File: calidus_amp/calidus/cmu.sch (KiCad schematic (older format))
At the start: 21 parts, among them Q1 Q_NPN_CBE, Q2 Q_NPN_CBE, Q3 Q_NPN_CBE, U6 PIC18F26K40_ISP

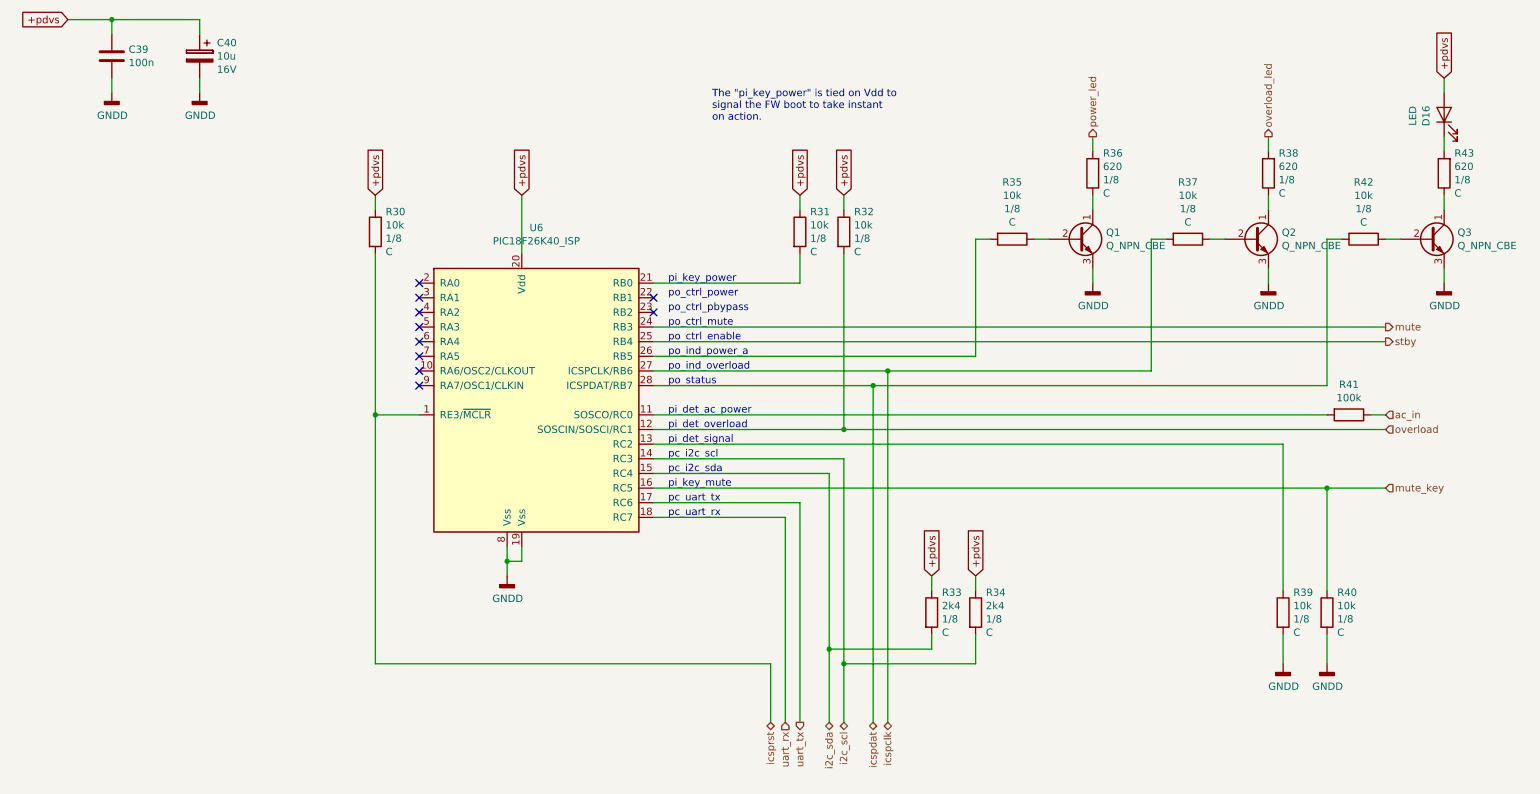
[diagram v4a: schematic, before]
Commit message: WIP: Component placement on PCB
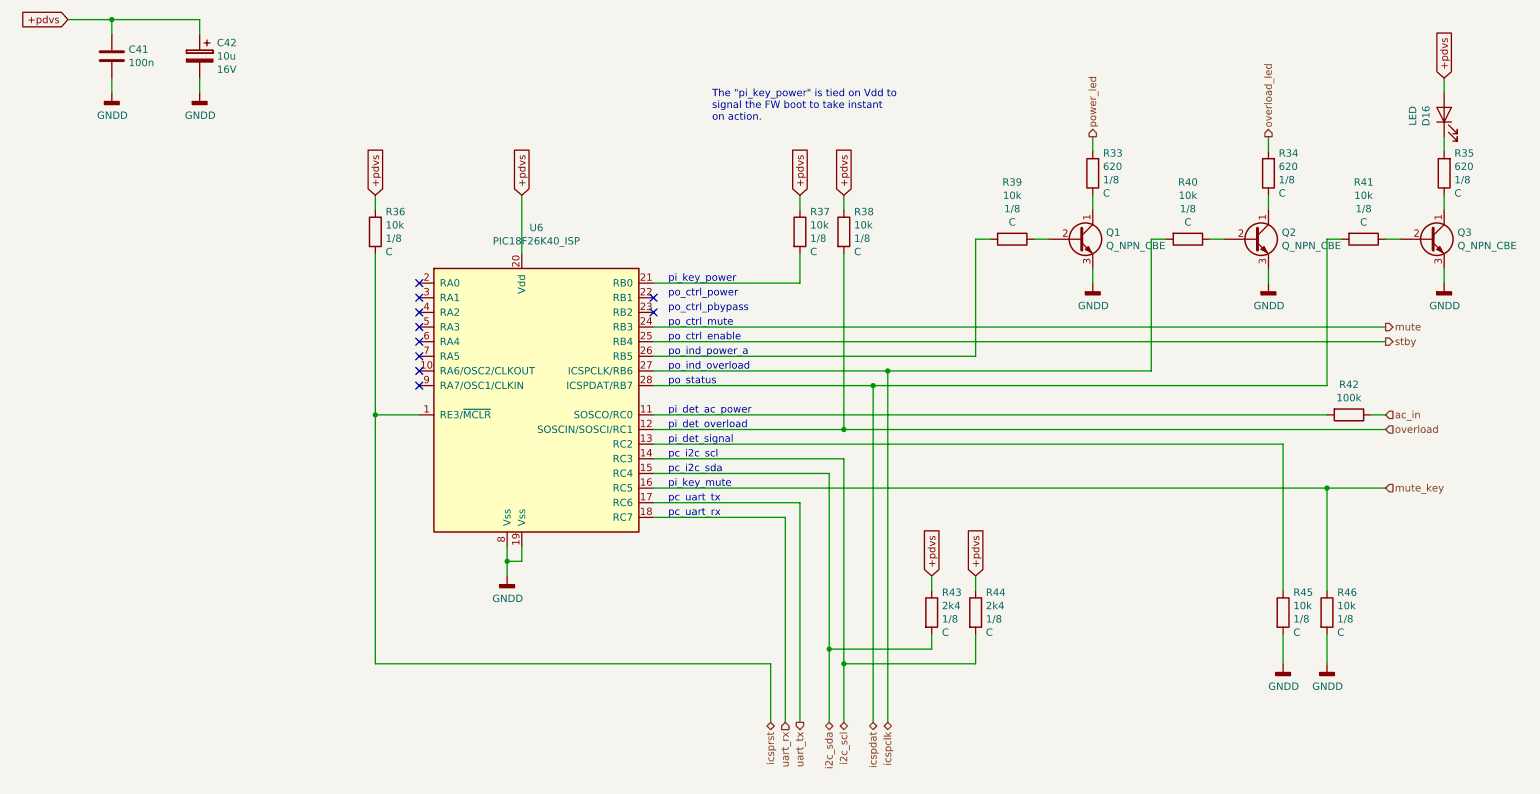
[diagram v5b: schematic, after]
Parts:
- renumbered C39 to C41, C40 to C42, R36 to R33, R38 to R34, R43 to R35, R30 to R36, R31 to R37, R32 to R38, R35 to R39, R37 to R40, R42 to R41, R41 to R42, R33 to R43, R34 to R44, R39 to R45, R40 to R46
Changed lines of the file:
@@
 $Descr A4 11693 8268
 encoding utf-8
-Sheet 5 4
+Sheet 4 4
 Title ""
 Date ""
@@
 $EndDescr
 $Comp
-L power:GNDD #PWR031
+L power:GNDD #PWR028
 U 1 1 5C444574
 P 4200 5200
-F 0 "#PWR031" H 4200 4950 50  0001 C CNN
+F 0 "#PWR028" H 4200 4950 50  0001 C CNN
 F 1 "GNDD" H 4204 5045 50  0000 C CNN
 F 2 "" H 4200 5200 50  0001 C CNN
@@
 	1500 1400 1500 1500
 $Comp
-L power:GNDD #PWR029
+L power:GNDD #PWR023
 U 1 1 5C444792
 P 1500 1900
-F 0 "#PWR029" H 1500 1650 50  0001 C CNN
+F 0 "#PWR023" H 1500 1650 50  0001 C CNN
 F 1 "GNDD" H 1504 1745 50  0000 C CNN
 F 2 "" H 1500 1900 50  0001 C CNN
@@
 $EndComp
 $Comp
-L Device:C C39
+L Device:C C41
 U 1 1 5C46D3BF
 P 1500 1650
-F 0 "C39" H 1615 1696 50  0000 L CNN
+F 0 "C41" H 1615 1696 50  0000 L CNN
 F 1 "100n" H 1615 1605 50  0000 L CNN
 F 2 "Capacitor_THT:C_Rect_L7.0mm_W2.5mm_P5.00mm" H 1538 1500 50  0001 C CNN
@@
 NoConn ~ 5200 3300
 $Comp
-L Device:R R36
+L Device:R R33
 U 1 1 5C48301D
 P 8200 2450
-F 0 "R36" H 8130 2313 50  0000 R CNN
+F 0 "R33" H 8130 2313 50  0000 R CNN
 F 1 "620" H 8130 2404 50  0000 R CNN
 F 2 "Resistor_THT:R_Axial_DIN0204_L3.6mm_D1.6mm_P5.08mm_Horizontal" V 8130 2450 50  0001 C CNN
@@
 $EndComp
 $Comp
-L power:GNDD #PWR032
+L power:GNDD #PWR025
 U 1 1 5C4835A2
 P 8200 3200
-F 0 "#PWR032" H 8200 2950 50  0001 C CNN
+F 0 "#PWR025" H 8200 2950 50  0001 C CNN
 F 1 "GNDD" H 8204 3045 50  0000 C CNN
 F 2 "" H 8200 3200 50  0001 C CNN
@@
 	8200 3200 8200 3100
 $Comp
-L power:GNDD #PWR033
+L power:GNDD #PWR026
 U 1 1 5C46343D
 P 9400 3200
-F 0 "#PWR033" H 9400 2950 50  0001 C CNN
+F 0 "#PWR026" H 9400 2950 50  0001 C CNN
 F 1 "GNDD" H 9404 3045 50  0000 C CNN
 F 2 "" H 9400 3200 50  0001 C CNN
@@
 $EndComp
 $Comp
-L power:GNDD #PWR036
+L power:GNDD #PWR027
 U 1 1 5C463464
 P 10600 3200
-F 0 "#PWR036" H 10600 2950 50  0001 C CNN
+F 0 "#PWR027" H 10600 2950 50  0001 C CNN
 F 1 "GNDD" H 10604 3045 50  0000 C CNN
 F 2 "" H 10600 3200 50  0001 C CNN
@@
 	9800 2900 9900 2900
 $Comp
-L Device:R R30
+L Device:R R36
 U 1 1 5C4640C2
 P 3300 2850
-F 0 "R30" H 3370 2987 50  0000 L CNN
+F 0 "R36" H 3370 2987 50  0000 L CNN
 F 1 "10k" H 3370 2896 50  0000 L CNN
 F 2 "Resistor_THT:R_Axial_DIN0204_L3.6mm_D1.6mm_P5.08mm_Horizontal" V 3230 2850 50  0001 C CNN
@@
 	10200 4200 6500 4200
 $Comp
-L Device:R R41
+L Device:R R42
 U 1 1 5C466052
 P 9950 4100
-F 0 "R41" V 9743 4100 50  0000 C CNN
+F 0 "R42" V 9743 4100 50  0000 C CNN
 F 1 "100k" V 9834 4100 50  0000 C CNN
 F 2 "Resistor_THT:R_Axial_DIN0207_L6.3mm_D2.5mm_P7.62mm_Horizontal" V 9880 4100 50  0001 C CNN
@@
 	6500 4400 5200 4400
 $Comp
-L power:GNDD #PWR034
+L power:GNDD #PWR029
 U 1 1 5C475E16
 P 9500 5800
-F 0 "#PWR034" H 9500 5550 50  0001 C CNN
+F 0 "#PWR029" H 9500 5550 50  0001 C CNN
 F 1 "GNDD" H 9504 5645 50  0000 C CNN
 F 2 "" H 9500 5800 50  0001 C CNN
@@
 $EndComp
 $Comp
-L power:GNDD #PWR035
+L power:GNDD #PWR030
 U 1 1 5C476CD2
 P 9800 5800
-F 0 "#PWR035" H 9800 5550 50  0001 C CNN
+F 0 "#PWR030" H 9800 5550 50  0001 C CNN
 F 1 "GNDD" H 9804 5645 50  0000 C CNN
 F 2 "" H 9800 5800 50  0001 C CNN
@@
 $EndComp
 $Comp
-L Device:R R33
+L Device:R R43
 U 1 1 5C477BD2
 P 7100 5450
-F 0 "R33" H 7170 5587 50  0000 L CNN
+F 0 "R43" H 7170 5587 50  0000 L CNN
 F 1 "2k4" H 7170 5496 50  0000 L CNN
 F 2 "Resistor_THT:R_Axial_DIN0204_L3.6mm_D1.6mm_P5.08mm_Horizontal" V 7030 5450 50  0001 C CNN
@@
 	6500 4200 5200 4200
 $Comp
-L Device:R R31
+L Device:R R37
 U 1 1 5C4C2301
 P 6200 2850
-F 0 "R31" H 6270 2987 50  0000 L CNN
+F 0 "R37" H 6270 2987 50  0000 L CNN
 F 1 "10k" H 6270 2896 50  0000 L CNN
 F 2 "Resistor_THT:R_Axial_DIN0204_L3.6mm_D1.6mm_P5.08mm_Horizontal" V 6130 2850 50  0001 C CNN
@@
 $EndComp
 $Comp
-L Device:R R32
+L Device:R R38
 U 1 1 5C4C234B
 P 6500 2850
-F 0 "R32" H 6570 2987 50  0000 L CNN
+F 0 "R38" H 6570 2987 50  0000 L CNN
 F 1 "10k" H 6570 2896 50  0000 L CNN
 F 2 "Resistor_THT:R_Axial_DIN0204_L3.6mm_D1.6mm_P5.08mm_Horizontal" V 6430 2850 50  0001 C CNN
@@
 $EndComp
 $Comp
-L Device:R R39
+L Device:R R45
 U 1 1 5C4C2657
 P 9500 5450
-F 0 "R39" H 9570 5587 50  0000 L CNN
+F 0 "R45" H 9570 5587 50  0000 L CNN
 F 1 "10k" H 9570 5496 50  0000 L CNN
 F 2 "Resistor_THT:R_Axial_DIN0204_L3.6mm_D1.6mm_P5.08mm_Horizontal" V 9430 5450 50  0001 C CNN
@@
 $EndComp
 $Comp
-L Device:R R40
+L Device:R R46
 U 1 1 5C4C26B7
 P 9800 5450
-F 0 "R40" H 9870 5587 50  0000 L CNN
+F 0 "R46" H 9870 5587 50  0000 L CNN
 F 1 "10k" H 9870 5496 50  0000 L CNN
 F 2 "Resistor_THT:R_Axial_DIN0204_L3.6mm_D1.6mm_P5.08mm_Horizontal" V 9730 5450 50  0001 C CNN
@@
 $EndComp
 $Comp
-L Device:R R35
+L Device:R R39
 U 1 1 5C4C2732
 P 7650 2900
-F 0 "R35" V 7261 2900 50  0000 C CNN
+F 0 "R39" V 7261 2900 50  0000 C CNN
 F 1 "10k" V 7352 2900 50  0000 C CNN
 F 2 "Resistor_THT:R_Axial_DIN0204_L3.6mm_D1.6mm_P5.08mm_Horizontal" V 7580 2900 50  0001 C CNN
@@
 $EndComp
 $Comp
-L Device:R R37
+L Device:R R40
 U 1 1 5C4C2878
 P 8850 2900
-F 0 "R37" V 8461 2900 50  0000 C CNN
+F 0 "R40" V 8461 2900 50  0000 C CNN
 F 1 "10k" V 8552 2900 50  0000 C CNN
 F 2 "Resistor_THT:R_Axial_DIN0204_L3.6mm_D1.6mm_P5.08mm_Horizontal" V 8780 2900 50  0001 C CNN
@@
 $EndComp
 $Comp
-L Device:R R42
+L Device:R R41
 U 1 1 5C4C28CE
 P 10050 2900
-F 0 "R42" V 9661 2900 50  0000 C CNN
+F 0 "R41" V 9661 2900 50  0000 C CNN
 F 1 "10k" V 9752 2900 50  0000 C CNN
 F 2 "Resistor_THT:R_Axial_DIN0204_L3.6mm_D1.6mm_P5.08mm_Horizontal" V 9980 2900 50  0001 C CNN
@@
 P 2100 1650
 AR Path="/5C37BC7C/5C4C9FCF" Ref="C?"  Part="1"
-AR Path="/5C43C4AB/5C4C9FCF" Ref="C40"  Part="1"
-F 0 "C40" H 1982 1741 50  0000 R CNN
+AR Path="/5C43C4AB/5C4C9FCF" Ref="C42"  Part="1"
+F 0 "C42" H 1982 1741 50  0000 R CNN
 F 1 "10u" H 1982 1650 50  0000 R CNN
 F 2 "Capacitor_THT:CP_Radial_D5.0mm_P2.00mm" H 2138 1500 50  0001 C CNN
@@
 $EndComp
 $Comp
-L power:GNDD #PWR030
+L power:GNDD #PWR024
 U 1 1 5C4CB7C3
 P 2100 1900
-F 0 "#PWR030" H 2100 1650 50  0001 C CNN
+F 0 "#PWR024" H 2100 1650 50  0001 C CNN
 F 1 "GNDD" H 2104 1745 50  0000 C CNN
 F 2 "" H 2100 1900 50  0001 C CNN
@@
 Connection ~ 1500 1400
 $Comp
-L Device:R R34
+L Device:R R44
 U 1 1 5C4F79CD
 P 7400 5450
-F 0 "R34" H 7470 5587 50  0000 L CNN
+F 0 "R44" H 7470 5587 50  0000 L CNN
 F 1 "2k4" H 7470 5496 50  0000 L CNN
 F 2 "Resistor_THT:R_Axial_DIN0204_L3.6mm_D1.6mm_P5.08mm_Horizontal" V 7330 5450 50  0001 C CNN
@@
 $EndComp
 $Comp
-L Device:R R38
+L Device:R R34
 U 1 1 5C4F9272
 P 9400 2450
-F 0 "R38" H 9330 2313 50  0000 R CNN
+F 0 "R34" H 9330 2313 50  0000 R CNN
 F 1 "620" H 9330 2404 50  0000 R CNN
 F 2 "Resistor_THT:R_Axial_DIN0204_L3.6mm_D1.6mm_P5.08mm_Horizontal" V 9330 2450 50  0001 C CNN
@@
 $EndComp
 $Comp
-L Device:R R43
+L Device:R R35
 U 1 1 5C4F92B8
 P 10600 2450
-F 0 "R43" H 10530 2313 50  0000 R CNN
+F 0 "R35" H 10530 2313 50  0000 R CNN
 F 1 "620" H 10530 2404 50  0000 R CNN
 F 2 "Resistor_THT:R_Axial_DIN0204_L3.6mm_D1.6mm_P5.08mm_Horizontal" V 10530 2450 50  0001 C CNN

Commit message: WIP: Component placement
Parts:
- renumbered C41 to C45, C42 to C46
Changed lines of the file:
@@
 $EndComp
 $Comp
-L Device:C C41
+L Device:C C45
 U 1 1 5C46D3BF
 P 1500 1650
-F 0 "C41" H 1615 1696 50  0000 L CNN
+F 0 "C45" H 1615 1696 50  0000 L CNN
 F 1 "100n" H 1615 1605 50  0000 L CNN
 F 2 "Capacitor_THT:C_Rect_L7.0mm_W2.5mm_P5.00mm" H 1538 1500 50  0001 C CNN
@@
 P 2100 1650
 AR Path="/5C37BC7C/5C4C9FCF" Ref="C?"  Part="1"
-AR Path="/5C43C4AB/5C4C9FCF" Ref="C42"  Part="1"
-F 0 "C42" H 1982 1741 50  0000 R CNN
+AR Path="/5C43C4AB/5C4C9FCF" Ref="C46"  Part="1"
+F 0 "C46" H 1982 1741 50  0000 R CNN
 F 1 "10u" H 1982 1650 50  0000 R CNN
 F 2 "Capacitor_THT:CP_Radial_D5.0mm_P2.00mm" H 2138 1500 50  0001 C CNN

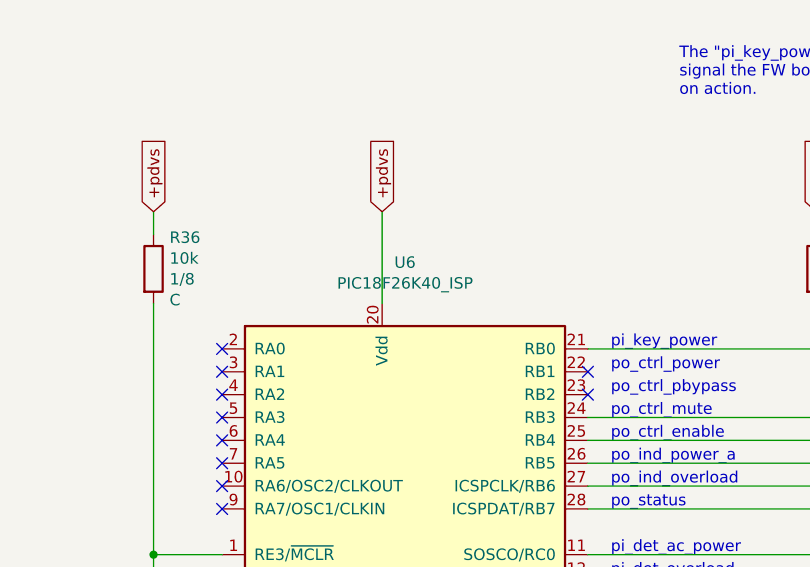
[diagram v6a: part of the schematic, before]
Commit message: WIP: Component placement and footprint assignement
- Finished all capacitors
- Finished all ICs
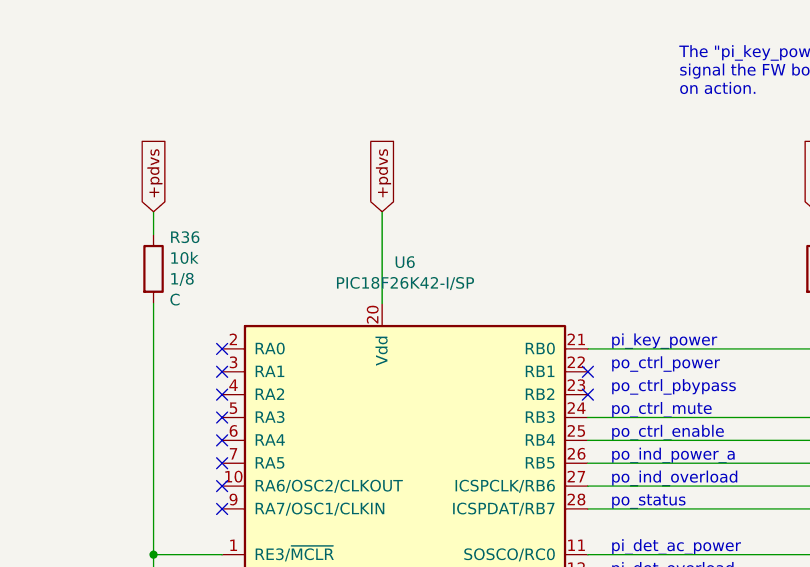
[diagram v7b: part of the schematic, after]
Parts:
- C45: footprint Capacitor_THT:C_Rect_L7.0mm_W2.5mm_P5.00mm -> Capacitor_THT:C_Rect_L4.6mm_W3.0mm_P2.50mm_MKS02_FKP02; Manufacturer (none) -> WIMA:MKS0C031000C00KSSD; Supplier1 (none) -> Farnell:1006004; Type (none) -> PET; Voltage (none) -> 63V
- R42: footprint Resistor_THT:R_Axial_DIN0207_L6.3mm_D2.5mm_P7.62mm_Horizontal -> Resistor_THT:R_Axial_DIN0204_L3.6mm_D1.6mm_P5.08mm_Horizontal; Manufacturer (none) -> Multicomp:MF12 10K; Power (none) -> 1/8; Supplier1 (none) -> Farnell:9342427; Type (none) -> C
- U6: value PIC18F26K40_ISP -> PIC18F26K42-I/SP; Manufacturer (none) -> Microchip:PIC18F26K42-I/SP; Supplier1 (none) -> Farnell:2835929
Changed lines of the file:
@@
 F 0 "C45" H 1615 1696 50  0000 L CNN
 F 1 "100n" H 1615 1605 50  0000 L CNN
-F 2 "Capacitor_THT:C_Rect_L7.0mm_W2.5mm_P5.00mm" H 1538 1500 50  0001 C CNN
-F 3 "~" H 1500 1650 50  0001 C CNN
+F 2 "Capacitor_THT:C_Rect_L4.6mm_W3.0mm_P2.50mm_MKS02_FKP02" H 1538 1500 50  0001 C CNN
+F 3 "http://www.farnell.com/datasheets/1306005.pdf" H 1500 1650 50  0001 C CNN
+F 4 "WIMA:MKS0C031000C00KSSD" H 0   0   50  0001 C CNN "Manufacturer"
+F 5 "Farnell:1006004" H 0   0   50  0001 C CNN "Supplier1"
+F 6 "PET" H 0   0   50  0001 C CNN "Type"
+F 7 "63V" H 0   0   50  0001 C CNN "Voltage"
 	1    1500 1650
 	1    0    0    -1
@@
 P 4400 4000
 F 0 "U6" H 4400 5178 50  0000 C CNN
-F 1 "PIC18F26K40_ISP" H 4400 5087 50  0000 C CNN
+F 1 "PIC18F26K42-I/SP" H 4400 5087 50  0000 C CNN
 F 2 "Package_DIP:DIP-28_W7.62mm_LongPads" H 3900 3500 50  0001 C CNN
 F 3 "http://ww1.microchip.com/downloads/en/DeviceDoc/PIC18LF26-45-46K40-Data-Sheet-DS40001816F.pdf" H 4400 3950 50  0001 C CNN
+F 4 "Microchip:PIC18F26K42-I/SP" H 0   0   50  0001 C CNN "Manufacturer"
+F 5 "Farnell:2835929" H 0   0   50  0001 C CNN "Supplier1"
 	1    4400 4000
 	1    0    0    -1
@@
 F 0 "R42" V 9743 4100 50  0000 C CNN
 F 1 "100k" V 9834 4100 50  0000 C CNN
-F 2 "Resistor_THT:R_Axial_DIN0207_L6.3mm_D2.5mm_P7.62mm_Horizontal" V 9880 4100 50  0001 C CNN
-F 3 "~" H 9950 4100 50  0001 C CNN
+F 2 "Resistor_THT:R_Axial_DIN0204_L3.6mm_D1.6mm_P5.08mm_Horizontal" V 9880 4100 50  0001 C CNN
+F 3 "http://www.farnell.com/datasheets/1716726.pdf" H 9950 4100 50  0001 C CNN
+F 4 "Multicomp:MF12 10K" H 0   0   50  0001 C CNN "Manufacturer"
+F 5 "1/8" H 0   0   50  0001 C CNN "Power"
+F 6 "Farnell:9342427" H 0   0   50  0001 C CNN "Supplier1"
+F 7 "C" H 0   0   50  0001 C CNN "Type"
 	1    9950 4100
 	0    1    1    0
